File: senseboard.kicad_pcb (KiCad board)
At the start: 6 copper layers, 60 x 100 mm, 87 parts, among them J1 USB_C_Receptacle_USB2.0_16P, J2 Screw_Terminal_01x02, J3 DM3AT-SF-PEJM5, J4 Conn_01x04, J5 Conn_01x08, U1 USBLC6-2SC6, U10 EMIF06-MSD02N16, U11 BME690, U2 TPS62840DLCR, U3 TPS62840DLCR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

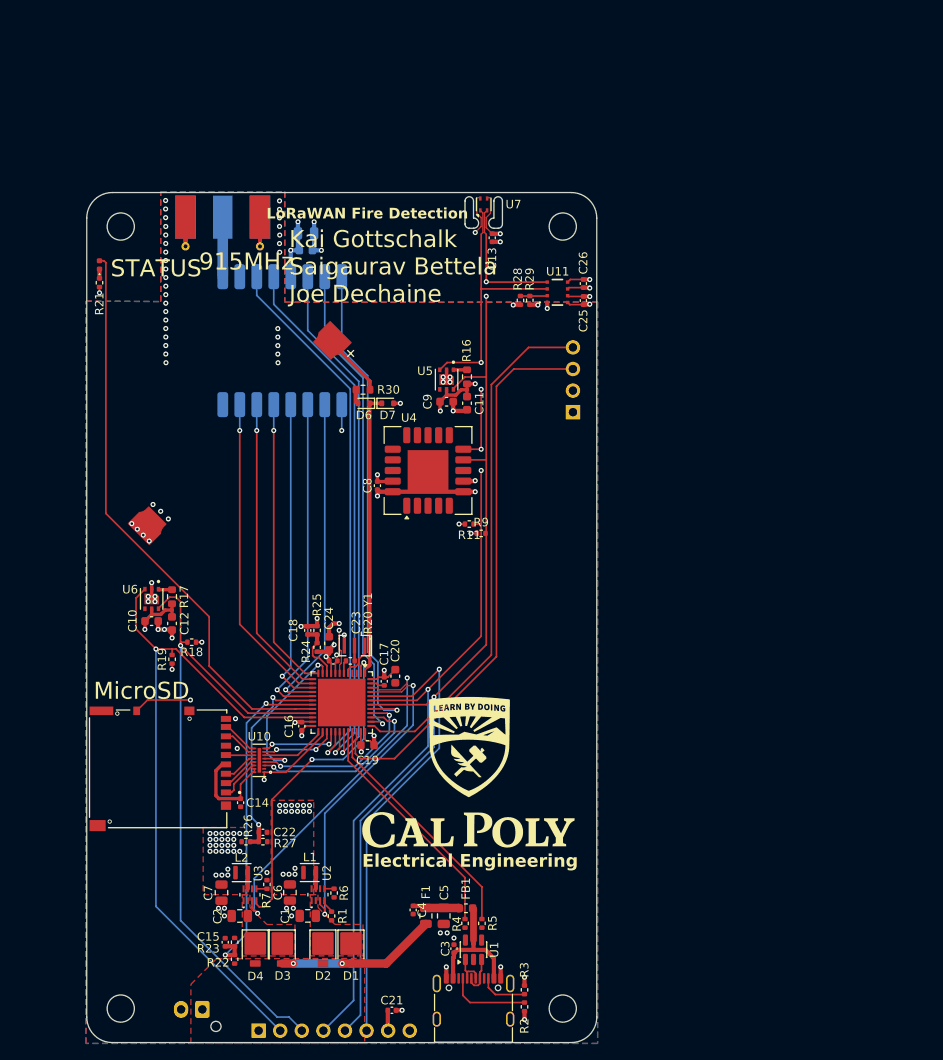
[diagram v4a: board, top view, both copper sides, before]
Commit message: added lots of additional resistors and caps for added decoupling and modification if neccesary, finalized layout and added graphics
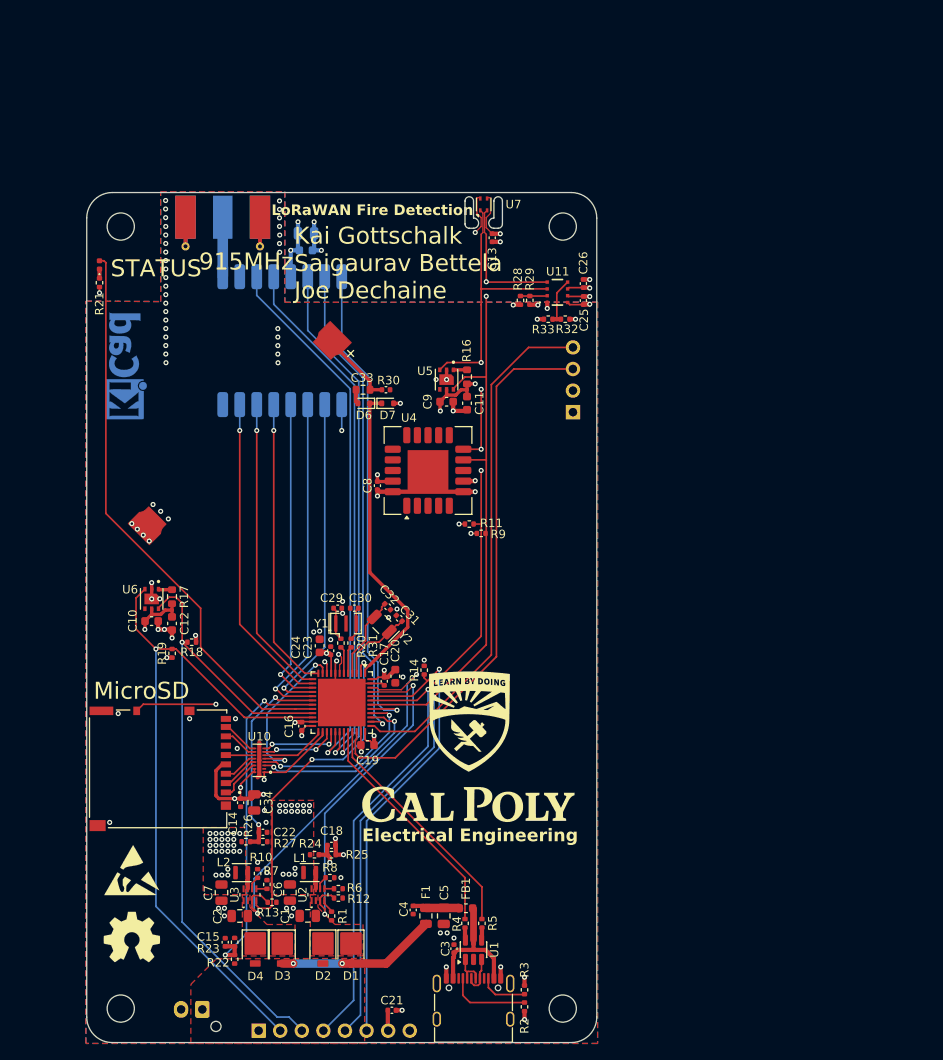
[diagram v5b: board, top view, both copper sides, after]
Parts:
- added C29: 33pF, Capacitor_SMD:C_0402_1005Metric, F.Cu at (109.5, 118.9)
- added C30: 33pF, Capacitor_SMD:C_0402_1005Metric, F.Cu at (111.5, 118.9)
- added C31: 33pF, Capacitor_SMD:C_0402_1005Metric, F.Cu at (116.8, 120.1)
- added C32: 33pF, Capacitor_SMD:C_0402_1005Metric, F.Cu at (115.4, 118.7)
- added C33: 0.1uF, Capacitor_SMD:C_0402_1005Metric, F.Cu at (115.2, 93.2)
- added C34: 10uF, Capacitor_SMD:C_0805_2012Metric, F.Cu at (99.7, 141.8)
- added R10: 0, Resistor_SMD:R_0402_1005Metric, F.Cu at (100.1, 150.1)
- added R12: 0, Resistor_SMD:R_0402_1005Metric, F.Cu at (109.6, 153.0)
- added R13: 0, Resistor_SMD:R_0402_1005Metric, F.Cu at (101.8, 153.5)
- added R14: 0, Resistor_SMD:R_0402_1005Metric, F.Cu at (119.7, 126.2)
- added R31: 0, Resistor_SMD:R_0402_1005Metric, F.Cu at (111.1, 123.0)
- added R32: 0, Resistor_SMD:R_0402_1005Metric, F.Cu at (136.3, 84.9)
- added R33: 0, Resistor_SMD:R_0402_1005Metric, F.Cu at (134.3, 84.9)
- added R8: 0, Resistor_SMD:R_0402_1005Metric, F.Cu at (108.6, 150.6)
- added REF**: OSHW-Symbol_6.7x6mm_SilkScreen, Symbol:OSHW-Symbol_6.7x6mm_SilkScreen, F.Cu at (85.3, 157.6)
- added REF**: ESD-Logo_6.6x6mm_SilkScreen, Symbol:ESD-Logo_6.6x6mm_SilkScreen, F.Cu at (85.3, 149.7)
- added REF**: KiCad-Logo_5mm_Copper, Symbol:KiCad-Logo_5mm_Copper, B.Cu at (84.1, 90.4)
- added Y2: Crystal, Crystal:Crystal_SMD_EuroQuartz_EQ161-2Pin_3.2x1.5mm, F.Cu at (114.7, 120.8)
- D6, D7: value D_Schottky -> BAT54WX-TP
- R20: value TBD -> 0
- R30: value 4.7 -> 330
- U2, U3: value TPS62840DLCR -> TPS62849DLCR; footprint TPS62840DLCR:VSON8_2P1X1P6_TEX -> TPS62849DLCR:VSON8_2P1X1P6_TEX
- moved R25 26.4 mm to (108.8, 147.9), turned to 0 degrees
- moved C18 25.4 mm to (108.8, 146.8), turned to 0 degrees
- moved R24 24.4 mm to (106.8, 147.9), turned to 0 degrees
- moved G*** 3.00 mm to (124.9, 135.2)
- moved Y1 2.79 mm to (110.5, 120.7), turned to 0 degrees
- moved R20 2.38 mm to (109.9, 123.0), turned to 90 degrees
- moved C23 1.24 mm to (108.7, 123.9), turned to -90 degrees
- moved C24 1.14 mm to (107.4, 123.3)
- moved R6 0.71 mm to (109.6, 151.9), turned to 0 degrees
- moved R19 0.70 mm to (90.0, 124.2)
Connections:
- net /GPIO_EX renamed /GPIO_EX/BOOT0
- R20 pad 2: Net-(R20-Pad2) -> Net-(C29-Pad1)
- U11 pad 5: GND -> /SDO
- U2 pad 6: unconnected-(U2-STOP-Pad6) -> /3V3_STOP1
- U3 pad 6: unconnected-(U3-STOP-Pad6) -> /3V3_STOP2
- U8 pad 3: unconnected-(U8-PC14-Pad3) -> /OSC32_IN
- U8 pad 4: unconnected-(U8-PC15-Pad4) -> /OSC32_OUT
- Y1 pad 1: Net-(U8-PH0) -> Net-(C29-Pad1)
- Y1 pad 2: Net-(R20-Pad2) -> GND
- Y1 pad 3: GND -> Net-(C30-Pad2)
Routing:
- net /VSENSE_3V3_1: track 6.85 -> 28.7 mm, vias 0 -> 2
- net GND: track 62.6 -> 78.7 mm, vias 91 -> 99
- net /OSC32_OUT: track 0.00 -> 9.75 mm
- net /OSC32_IN: track 0.00 -> 9.23 mm
- net /SDO: track 0.00 -> 5.87 mm
- net /RESET: track 57.3 -> 51.6 mm
- net /3V3_MODE2: track 42.4 -> 46.9 mm
- net Net-(C30-Pad2): track 0.00 -> 3.95 mm
- net Net-(C29-Pad1): track 0.00 -> 3.95 mm
- net Net-(D6-K): track 33.4 -> 37.1 mm
- net /3V3_MODE1: track 38.3 -> 40.5 mm
- net /SDMMC_DET: track 34.0 -> 31.8 mm
- net +3V3_1: track 50.8 -> 52.7 mm, vias 32 -> 35
- net Net-(R20-Pad2): track 1.80 -> 0.00 mm
- net Net-(U8-PH1): track 1.56 -> 3.20 mm
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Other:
- rule pad_to_mask_clearance: 0.09 -> 0
